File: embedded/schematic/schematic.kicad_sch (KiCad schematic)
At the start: 4 parts

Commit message: Updated schematics
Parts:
- removed C1: 100n, Capacitor_THT:C_Rect_L9.0mm_W2.5mm_P7.50mm_MKT, symbol Device:C
- removed V1: 7.4, symbol Simulation_SPICE:VDC
- added BuckBoost3.3V1: ~, custom:BuckBoost3.3V, symbol custom:BuckBoost3.3V
- added Q1: AO3400A, Package_TO_SOT_SMD:SOT-23, symbol Transistor_FET:AO3400A
- added R3: 4.7k, Resistor_THT:R_Axial_DIN0207_L6.3mm_D2.5mm_P10.16mm_Horizontal, symbol Device:R
- R1: value 2M -> 1M; footprint Resistor_THT:R_Axial_DIN0204_L3.6mm_D1.6mm_P7.62mm_Horizontal -> Resistor_THT:R_Axial_DIN0207_L6.3mm_D2.5mm_P10.16mm_Horizontal
- R2: footprint Resistor_THT:R_Axial_DIN0204_L3.6mm_D1.6mm_P7.62mm_Horizontal -> Resistor_THT:R_Axial_DIN0207_L6.3mm_D2.5mm_P10.16mm_Horizontal
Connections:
- net GND: now also BuckBoost3.3V1.1 (Vout-), Q1.2 (S); no longer R2.2
- net BAT+: now reaches R1.1
- net BAT+: now also BuckBoost3.3V1.2 (Vin+), BuckBoost3.3V1.3 (EN)
- net BAT: now reaches R1.2, R2.1
- new net: Q1.3 (D), R2.2
- new net 3.3V: BuckBoost3.3V1.4 (Vout+)
- new net SEN: Q1.1 (G), R3.1
- new net TMP: R3.2

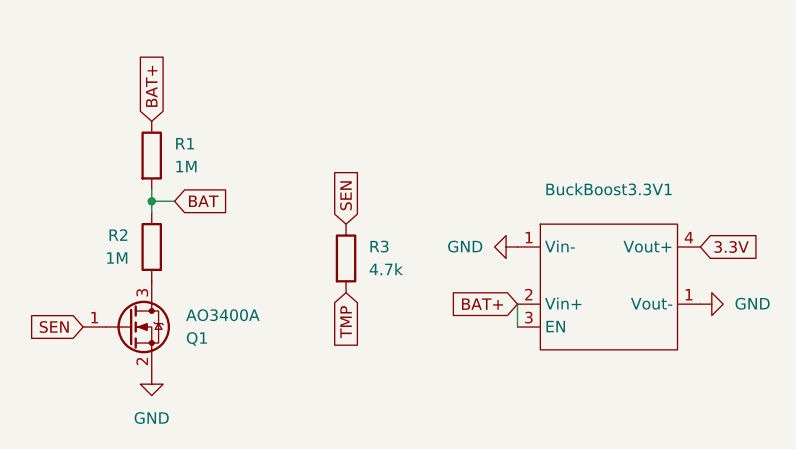
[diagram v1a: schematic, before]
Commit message: Added compact schematic
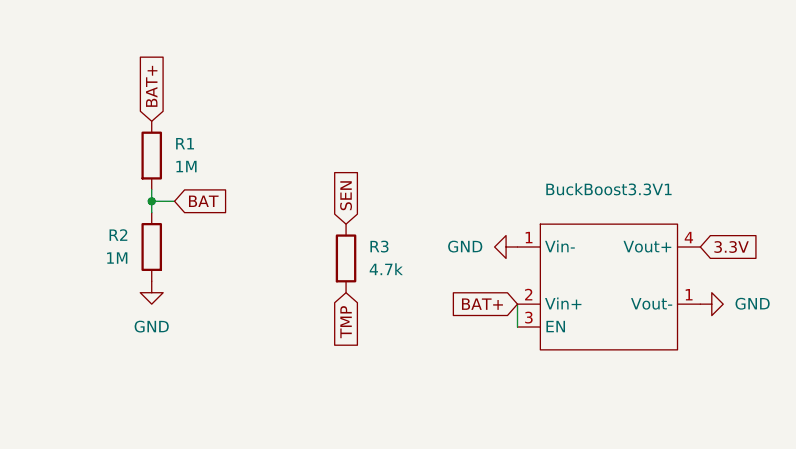
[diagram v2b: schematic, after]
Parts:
- removed Q1: AO3400A, Package_TO_SOT_SMD:SOT-23, symbol Transistor_FET:AO3400A
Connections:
- net GND: now also R2.2
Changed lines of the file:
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@@
-		)
-	)
-	(global_label "SEN"
-		(shape input)
-		(at 22.86 48.26 180)
-		(fields_autoplaced yes)
-		(effects
-			(font
-				(size 1.27 1.27)
-			)
-			(justify right)
-		)
-		(property "Intersheetrefs" "${INTERSHEET_REFS}"
-			(at 16.1858 48.26 0)
-			(effects
-				(font
-					(size 1.27 1.27)
-				)
-				(justify right)
-				(hide yes)
-			)
 		)
 	)
@@
 	(symbol
 		(lib_id "power:GND")
-		(at 30.48 53.34 0)
+		(at 30.48 43.18 0)
 		(unit 1)
 		(exclude_from_sim no)
@@
 		(fields_autoplaced yes)
 		(property "Reference" "#PWR01"
-			(at 30.48 59.69 0)
+			(at 30.48 49.53 0)
 			(effects
 				(font
@@
 		)
 		(property "Value" "GND"
-			(at 30.48 58.42 0)
+			(at 30.48 48.26 0)
 			(effects
 				(font
@@
 		)
 		(property "Footprint" ""
-			(at 30.48 53.34 0)
+			(at 30.48 43.18 0)
 			(effects
 				(font
@@
 		)
 		(property "Datasheet" ""
-			(at 30.48 53.34 0)
+			(at 30.48 43.18 0)
 			(effects
 				(font
@@
 		)
 		(property "Description" "Power symbol creates a global label with name \"GND\" , ground"
-			(at 30.48 53.34 0)
+			(at 30.48 43.18 0)
 			(effects
 				(font
@@
 					(unit 1)
 				)
-			)
-		)
-	)
-	(symbol
-		(lib_id "Transistor_FET:AO3400A")
-		(at 27.94 48.26 0)
-		(unit 1)
-		(exclude_from_sim no)
-		(in_bom yes)
-		(on_board yes)
-		(dnp no)
-		(property "Reference" "Q1"
-			(at 34.29 49.5301 0)
-			(effects
-				(font
-					(size 1.27 1.27)
-				)
-				(justify left)
-			)
-		)
-		(property "Value" "AO3400A"
-			(at 34.29 46.9901 0)
-			(effects
-				(font
-					(size 1.27 1.27)
-				)
-				(justify left)
-			)
-		)
-		(property "Footprint" "Package_TO_SOT_SMD:SOT-23"
-			(at 33.02 50.165 0)
-			(effects
-				(font
-					(size 1.27 1.27)
-					(italic yes)
-				)
-				(justify left)
-				(hide yes)
-			)
-		)
-		(property "Datasheet" "http://www.aosmd.com/pdfs/datasheet/AO3400A.pdf"
-			(at 33.02 52.07 0)
-			(effects
-				(font
-					(size 1.27 1.27)
-				)
-				(justify left)
-				(hide yes)
-			)
-		)
-		(property "Description" "30V Vds, 5.7A Id, N-Channel MOSFET, SOT-23"
-			(at 27.94 48.26 0)
-			(effects
-				(font
-					(size 1.27 1.27)
-				)
-				(hide yes)
-			)
-		)
-		(pin "3"
-		)
-		(pin "2"
-		)
-		(pin "1"
-		)
-		(instances
-			(project ""
-				(path "/f9423e95-a155-48e4-a080-8587e4935509"
-					(reference "Q1")
-					(unit 1)
-				)
